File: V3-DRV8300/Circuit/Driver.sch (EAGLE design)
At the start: 37 parts, among them IC1 DRV8303DCA

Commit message: Prepared for V3-DRV8300 PCB routing
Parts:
- renumbered C10 to DVDD_CAP, C11 to AVDD_CAP
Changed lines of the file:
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@@
 <part name="SUPPLY3" library="supply2" library_urn="urn:adsk.eagle:library:372" deviceset="GND" device=""/>
 <part name="C9" library="SparkFun-Capacitors" deviceset="0.22UF" device="-0603-25V-10%" value="0.22uF"/>
-<part name="C10" library="SparkFun-Capacitors" deviceset="1.0UF" device="-0603-16V-10%" value="1.0uF"/>
+<part name="DVDD_CAP" library="SparkFun-Capacitors" deviceset="1.0UF" device="-0603-16V-10%" value="1.0uF"/>
 <part name="SUPPLY4" library="supply2" library_urn="urn:adsk.eagle:library:372" deviceset="GND" device=""/>
 <part name="P+4" library="supply1" library_urn="urn:adsk.eagle:library:371" deviceset="VCC" device=""/>
-<part name="C11" library="SparkFun-Capacitors" deviceset="1.0UF" device="-0603-16V-10%" value="1.0uF"/>
+<part name="AVDD_CAP" library="SparkFun-Capacitors" deviceset="1.0UF" device="-0603-16V-10%" value="1.0uF"/>
 <part name="SUPPLY10" library="supply2" library_urn="urn:adsk.eagle:library:372" deviceset="GND" device=""/>
 <part name="SUPPLY15" library="supply2" library_urn="urn:adsk.eagle:library:372" deviceset="GND" device=""/>
@@
 <attribute name="VALUE" x="212.979" y="128.524" size="1.778" layer="96" font="vector" rot="R90"/>
 </instance>
-<instance part="C10" gate="G$1" x="205.74" y="104.14" smashed="yes" rot="R90">
+<instance part="DVDD_CAP" gate="G$1" x="205.74" y="104.14" smashed="yes" rot="R90">
 <attribute name="NAME" x="202.819" y="105.664" size="1.778" layer="95" font="vector" rot="R90"/>
 <attribute name="VALUE" x="200.279" y="105.664" size="1.778" layer="96" font="vector" rot="R90"/>
@@
 <attribute name="VALUE" x="205.74" y="101.6" size="1.778" layer="96" rot="R180"/>
 </instance>
-<instance part="C11" gate="G$1" x="208.28" y="93.98" smashed="yes" rot="R270">
+<instance part="AVDD_CAP" gate="G$1" x="208.28" y="93.98" smashed="yes" rot="R270">
 <attribute name="NAME" x="211.201" y="92.456" size="1.778" layer="95" font="vector" rot="R270"/>
 <attribute name="VALUE" x="206.121" y="92.456" size="1.778" layer="96" font="vector" rot="R270"/>
@@
 </segment>
 <segment>
-<pinref part="C10" gate="G$1" pin="1"/>
+<pinref part="DVDD_CAP" gate="G$1" pin="1"/>
 <wire x1="200.66" y1="104.14" x2="198.12" y2="104.14" width="0.1524" layer="91"/>
 <pinref part="SUPPLY4" gate="GND" pin="GND"/>
@@
 <segment>
 <pinref part="IC1" gate="G$1" pin="AGND"/>
-<pinref part="C11" gate="G$1" pin="2"/>
+<pinref part="AVDD_CAP" gate="G$1" pin="2"/>
 <wire x1="205.74" y1="93.98" x2="205.74" y2="91.44" width="0.1524" layer="91"/>
 <wire x1="205.74" y1="91.44" x2="215.9" y2="91.44" width="0.1524" layer="91"/>
@@
 <segment>
 <pinref part="IC1" gate="G$1" pin="DVDD"/>
-<pinref part="C10" gate="G$1" pin="2"/>
+<pinref part="DVDD_CAP" gate="G$1" pin="2"/>
 <wire x1="215.9" y1="104.14" x2="208.28" y2="104.14" width="0.1524" layer="91"/>
 </segment>
@@
 <segment>
 <pinref part="IC1" gate="G$1" pin="AVDD"/>
-<pinref part="C11" gate="G$1" pin="1"/>
+<pinref part="AVDD_CAP" gate="G$1" pin="1"/>
 <wire x1="215.9" y1="93.98" x2="213.36" y2="93.98" width="0.1524" layer="91"/>
 </segment>

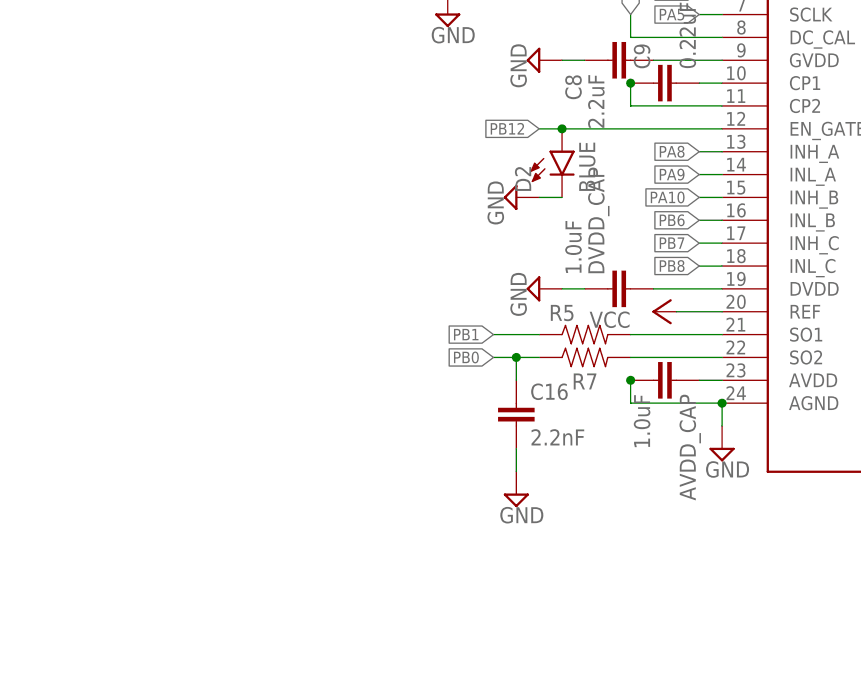
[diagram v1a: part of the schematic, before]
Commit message: Changed all the PWM output pin to the same timer, Added 2 selector for C.S.A.
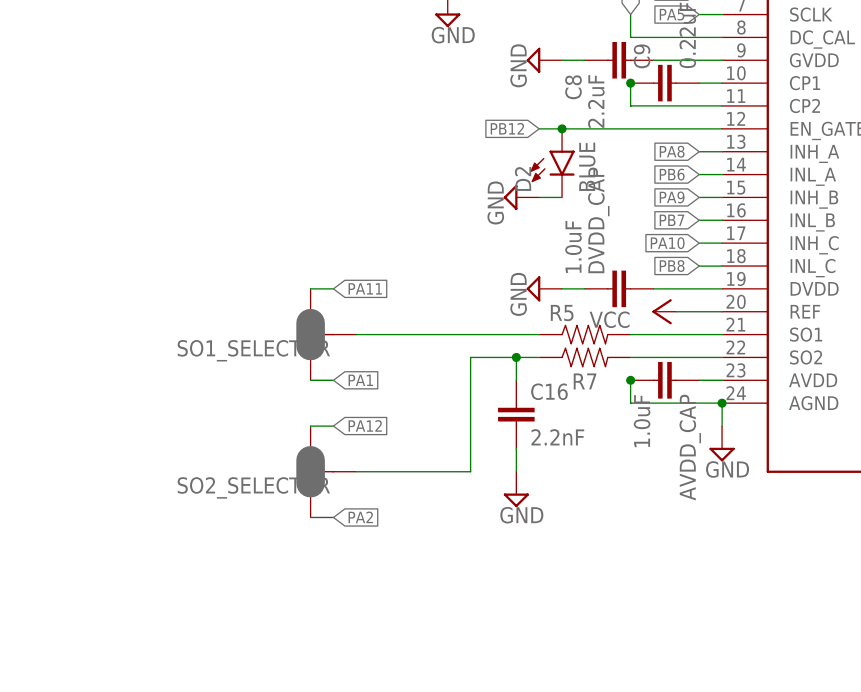
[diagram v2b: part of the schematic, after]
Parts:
- added SO1_SELECTOR, SO2_SELECTOR: JUMPER-SMT_3_2-NC_PASTE_SILK, SparkFun-Jumpers:JUMPER-SMT_3_2-NC_PASTE_SILK
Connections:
- new net SO1: R5.1, SO1_SELECTOR.2
- new net SO2: C16.1, R7.1, SO2_SELECTOR.2
- net PA1: now also SO1_SELECTOR.1
- net PA10: now also IC1.INH_C; no longer IC1.INH_B
- net PA11: now also SO1_SELECTOR.3
- net PA12: now also SO2_SELECTOR.3
- net PA2: now also SO2_SELECTOR.1
- net PA9: now also IC1.INH_B; no longer IC1.INL_A
- net PB0: no longer C16.1, R7.1
- net PB1: no longer R5.1
- net PB6: now also IC1.INL_A; no longer IC1.INL_B
- net PB7: now also IC1.INL_B; no longer IC1.INH_C
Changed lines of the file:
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@@
 <part name="SUPPLY24" library="supply2" library_urn="urn:adsk.eagle:library:372" deviceset="GND" device=""/>
 <part name="C16" library="SparkFun-Capacitors" deviceset="2.2NF/2200PF" device="-0603-50V-10%" value="2.2nF"/>
+<part name="SO1_SELECTOR" library="SparkFun-Jumpers" deviceset="JUMPER-SMT_3_2-NC_PASTE" device="_SILK" package3d_urn="urn:adsk.eagle:package:39294/1"/>
+<part name="SO2_SELECTOR" library="SparkFun-Jumpers" deviceset="JUMPER-SMT_3_2-NC_PASTE" device="_SILK" package3d_urn="urn:adsk.eagle:package:39294/1"/>
 </parts>
 <sheets>
@@
 <attribute name="NAME" x="194.564" y="91.821" size="1.778" layer="95" font="vector"/>
 <attribute name="VALUE" x="194.564" y="86.741" size="1.778" layer="96" font="vector"/>
+</instance>
+<instance part="SO1_SELECTOR" gate="G$1" x="170.18" y="99.06" smashed="yes" rot="R180">
+<attribute name="NAME" x="163.83" y="97.536" size="1.778" layer="95" font="vector" rot="R180" align="center"/>
+</instance>
+<instance part="SO2_SELECTOR" gate="G$1" x="170.18" y="83.82" smashed="yes" rot="R180">
+<attribute name="NAME" x="163.83" y="82.296" size="1.778" layer="95" font="vector" rot="R180" align="center"/>
 </instance>
 </instances>
@@
 <label x="83.82" y="114.3" size="1.27" layer="95" xref="yes"/>
 </segment>
-<segment>
-<pinref part="R5" gate="G$1" pin="1"/>
-<wire x1="195.58" y1="99.06" x2="190.5" y2="99.06" width="0.1524" layer="91"/>
-<label x="190.5" y="99.06" size="1.27" layer="95" rot="R180" xref="yes"/>
-</segment>
 </net>
 <net name="PB0" class="0">
@@
 <label x="83.82" y="111.76" size="1.27" layer="95" xref="yes"/>
 </segment>
-<segment>
-<label x="190.5" y="96.52" size="1.27" layer="95" rot="R180" xref="yes"/>
-<wire x1="193.04" y1="96.52" x2="190.5" y2="96.52" width="0.1524" layer="91"/>
-<wire x1="193.04" y1="96.52" x2="193.04" y2="93.98" width="0.1524" layer="91"/>
-<pinref part="C16" gate="G$1" pin="1"/>
-<pinref part="R7" gate="G$1" pin="1"/>
-<wire x1="195.58" y1="96.52" x2="193.04" y2="96.52" width="0.1524" layer="91"/>
-<junction x="193.04" y="96.52"/>
-</segment>
 </net>
 <net name="PA7" class="0">
@@
 <label x="83.82" y="96.52" size="1.27" layer="95" xref="yes"/>
 </segment>
+<segment>
+<wire x1="170.18" y1="78.74" x2="172.72" y2="78.74" width="0.1524" layer="91"/>
+<label x="172.72" y="78.74" size="1.27" layer="95" xref="yes"/>
+<pinref part="SO2_SELECTOR" gate="G$1" pin="1"/>
+</segment>
 </net>
 <net name="PA1" class="0">
@@
 <wire x1="78.74" y1="93.98" x2="83.82" y2="93.98" width="0.1524" layer="91"/>
 <label x="83.82" y="93.98" size="1.27" layer="95" xref="yes"/>
+</segment>
+<segment>
+<wire x1="170.18" y1="93.98" x2="172.72" y2="93.98" width="0.1524" layer="91"/>
+<label x="172.72" y="93.98" size="1.27" layer="95" xref="yes"/>
+<pinref part="SO1_SELECTOR" gate="G$1" pin="1"/>
 </segment>
 </net>
@@
 </segment>
 <segment>
-<pinref part="IC1" gate="G$1" pin="INL_A"/>
-<wire x1="215.9" y1="116.84" x2="213.36" y2="116.84" width="0.1524" layer="91"/>
-<label x="213.36" y="116.84" size="1.27" layer="95" rot="R180" xref="yes"/>
+<pinref part="IC1" gate="G$1" pin="INH_B"/>
+<wire x1="215.9" y1="114.3" x2="213.36" y2="114.3" width="0.1524" layer="91"/>
+<label x="213.36" y="114.3" size="1.27" layer="95" rot="R180" xref="yes"/>
 </segment>
 </net>
@@
 </segment>
 <segment>
-<pinref part="IC1" gate="G$1" pin="INH_B"/>
-<wire x1="215.9" y1="114.3" x2="213.36" y2="114.3" width="0.1524" layer="91"/>
-<label x="213.36" y="114.3" size="1.27" layer="95" rot="R180" xref="yes"/>
+<pinref part="IC1" gate="G$1" pin="INH_C"/>
+<wire x1="215.9" y1="109.22" x2="213.36" y2="109.22" width="0.1524" layer="91"/>
+<label x="213.36" y="109.22" size="1.27" layer="95" rot="R180" xref="yes"/>
 </segment>
 </net>
@@
 <label x="33.02" y="111.76" size="1.27" layer="95" rot="R180" xref="yes"/>
 </segment>
+<segment>
+<wire x1="170.18" y1="104.14" x2="172.72" y2="104.14" width="0.1524" layer="91"/>
+<label x="172.72" y="104.14" size="1.27" layer="95" xref="yes"/>
+<pinref part="SO1_SELECTOR" gate="G$1" pin="3"/>
+</segment>
 </net>
 <net name="PA12" class="0">
@@
 <wire x1="38.1" y1="109.22" x2="33.02" y2="109.22" width="0.1524" layer="91"/>
 <label x="33.02" y="109.22" size="1.27" layer="95" rot="R180" xref="yes"/>
+</segment>
+<segment>
+<wire x1="170.18" y1="88.9" x2="172.72" y2="88.9" width="0.1524" layer="91"/>
+<label x="172.72" y="88.9" size="1.27" layer="95" xref="yes"/>
+<pinref part="SO2_SELECTOR" gate="G$1" pin="3"/>
 </segment>
 </net>
@@
 </segment>
 <segment>
+<pinref part="IC1" gate="G$1" pin="INL_A"/>
+<wire x1="215.9" y1="116.84" x2="213.36" y2="116.84" width="0.1524" layer="91"/>
+<label x="213.36" y="116.84" size="1.27" layer="95" rot="R180" xref="yes"/>
+</segment>
+</net>
+<net name="PB7" class="0">
+<segment>
+<pinref part="U$1" gate="G$1" pin="PB7"/>
+<wire x1="38.1" y1="93.98" x2="33.02" y2="93.98" width="0.1524" layer="91"/>
+<label x="33.02" y="93.98" size="1.27" layer="95" rot="R180" xref="yes"/>
+</segment>
+<segment>
 <pinref part="IC1" gate="G$1" pin="INL_B"/>
 <wire x1="215.9" y1="111.76" x2="213.36" y2="111.76" width="0.1524" layer="91"/>
 <label x="213.36" y="111.76" size="1.27" layer="95" rot="R180" xref="yes"/>
-</segment>
-</net>
-<net name="PB7" class="0">
-<segment>
-<pinref part="U$1" gate="G$1" pin="PB7"/>
-<wire x1="38.1" y1="93.98" x2="33.02" y2="93.98" width="0.1524" layer="91"/>
-<label x="33.02" y="93.98" size="1.27" layer="95" rot="R180" xref="yes"/>
-</segment>
-<segment>
-<pinref part="IC1" gate="G$1" pin="INH_C"/>
-<wire x1="215.9" y1="109.22" x2="213.36" y2="109.22" width="0.1524" layer="91"/>
-<label x="213.36" y="109.22" size="1.27" layer="95" rot="R180" xref="yes"/>
 </segment>
 </net>
@@
 </segment>
 </net>
+<net name="SO1" class="0">
+<segment>
+<pinref part="R5" gate="G$1" pin="1"/>
+<wire x1="195.58" y1="99.06" x2="175.26" y2="99.06" width="0.1524" layer="91"/>
+<pinref part="SO1_SELECTOR" gate="G$1" pin="2"/>
+</segment>
+</net>
+<net name="SO2" class="0">
+<segment>
+<wire x1="193.04" y1="96.52" x2="187.96" y2="96.52" width="0.1524" layer="91"/>
+<wire x1="193.04" y1="96.52" x2="193.04" y2="93.98" width="0.1524" layer="91"/>
+<pinref part="C16" gate="G$1" pin="1"/>
+<pinref part="R7" gate="G$1" pin="1"/>
+<wire x1="195.58" y1="96.52" x2="193.04" y2="96.52" width="0.1524" layer="91"/>
+<junction x="193.04" y="96.52"/>
+<wire x1="187.96" y1="96.52" x2="187.96" y2="83.82" width="0.1524" layer="91"/>
+<wire x1="187.96" y1="83.82" x2="175.26" y2="83.82" width="0.1524" layer="91"/>
+<pinref part="SO2_SELECTOR" gate="G$1" pin="2"/>
+</segment>
+</net>

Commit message: Fixed a little mistake/bug (PA2 -> PA0)
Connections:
- net PA0: now also SO2_SELECTOR.1
- net PA2: no longer SO2_SELECTOR.1
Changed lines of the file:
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@@
 <label x="83.82" y="96.52" size="1.27" layer="95" xref="yes"/>
-</segment>
-<segment>
-<wire x1="170.18" y1="78.74" x2="172.72" y2="78.74" width="0.1524" layer="91"/>
-<label x="172.72" y="78.74" size="1.27" layer="95" xref="yes"/>
-<pinref part="SO2_SELECTOR" gate="G$1" pin="1"/>
 </segment>
 </net>
@@
 <label x="83.82" y="91.44" size="1.27" layer="95" xref="yes"/>
 </segment>
+<segment>
+<wire x1="170.18" y1="78.74" x2="172.72" y2="78.74" width="0.1524" layer="91"/>
+<label x="172.72" y="78.74" size="1.27" layer="95" xref="yes"/>
+<pinref part="SO2_SELECTOR" gate="G$1" pin="1"/>
+</segment>
 </net>
